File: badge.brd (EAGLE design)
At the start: 90.7 x 92.4 mm, 177 parts, among them CN4 MicroUSB, IC3 MEGA8-AI, Q1 BSS138, Q2 BSS138, T1 MMUN2133LT1G, U1 TPS61090RSAR, U2 MCP73871, U3 LIS3DHTR, U4 MIC5225-3.3, Y1 16.00MHz

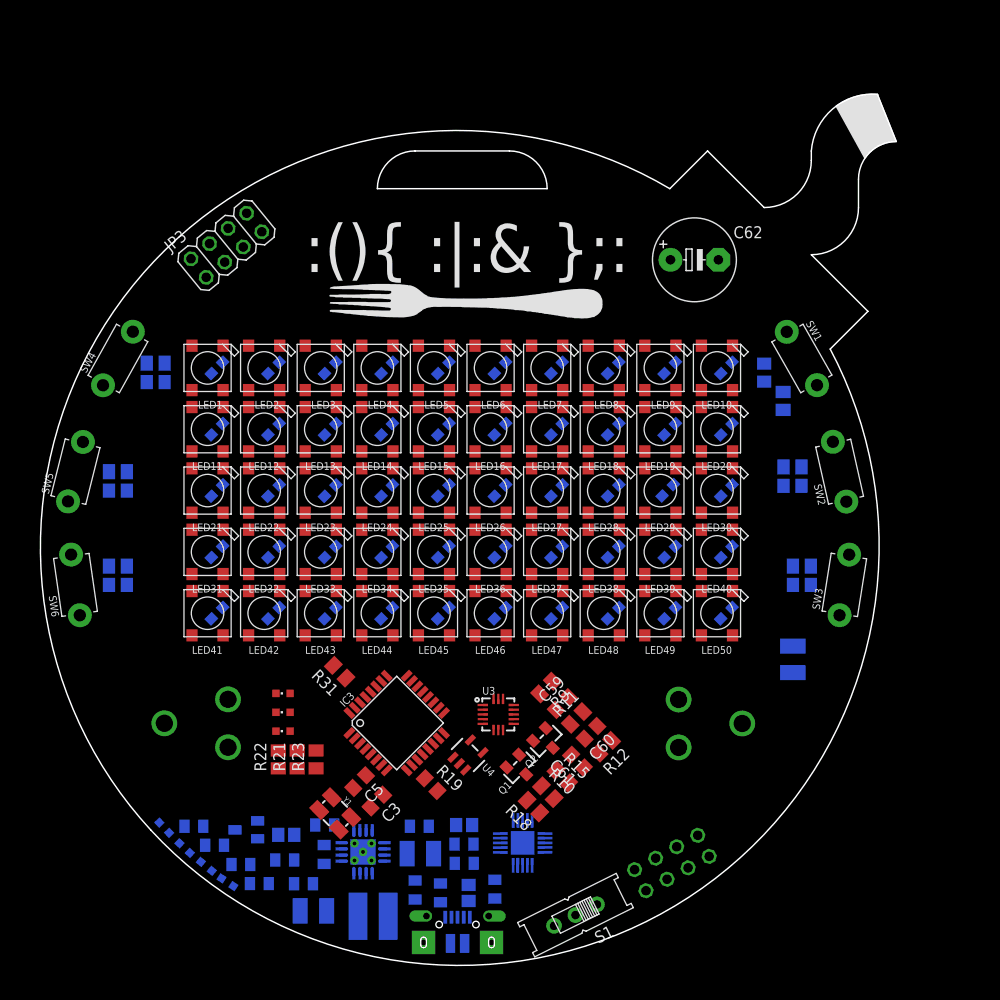
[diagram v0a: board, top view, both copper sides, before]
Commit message: Routed all the traces and performed a cursory DRC
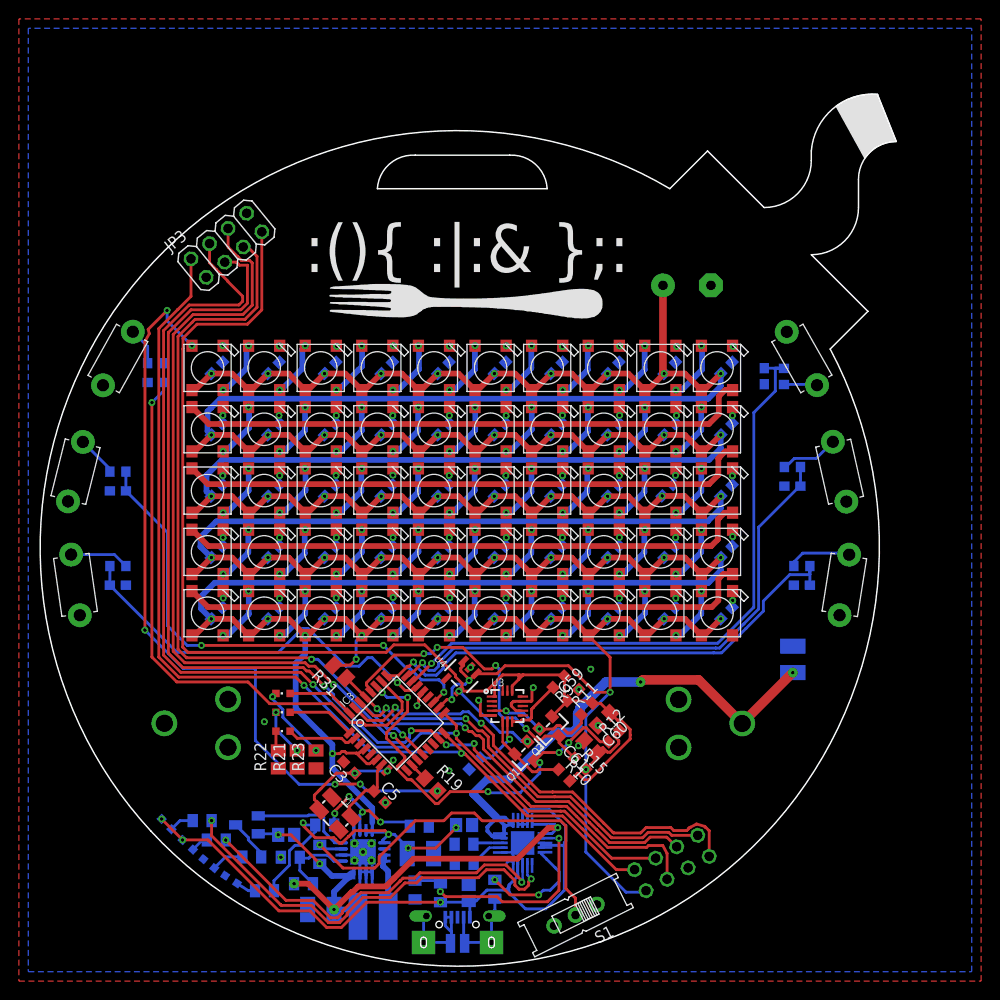
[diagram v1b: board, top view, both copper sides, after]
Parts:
- C3, C5, C59, C63, C64, C65, C66, C67, C68: device resistor:C0805 -> resistor:C0603
- R10, R11, R12, R15, R18, R24, R25, R26, R27, R28, R29, R9: device resistor:M0805 -> resistor:R0603
- moved U4 8.39 mm to (45.9, 31.3), turned to 135 degrees
- moved R18 7.70 mm to (47.3, 22.1), flipped to the bottom
- moved C3 4.61 mm to (34.0, 21.6), turned to 135 degrees
- moved C62 2.82 mm to (69.8, 72.8), flipped to the bottom, turned to 180 degrees
- moved C5 2.65 mm to (37.2, 18.5), turned to 315 degrees
- moved R24 2.60 mm to (80.1, 63.1)
- moved R10 2.50 mm to (56.8, 20.8)
- moved R15 2.33 mm to (58.5, 22.0)
- moved C61 2.05 mm to (59.6, 23.8)
- moved C60 1.94 mm to (61.0, 26.8)
- moved Q1 1.66 mm to (52.9, 23.0)
- moved R9 1.50 mm to (56.2, 30.7)
- moved R12 1.46 mm to (62.1, 25.0), turned to 45 degrees
- moved C59 1.45 mm to (57.7, 29.3)
- moved R11 1.45 mm to (59.2, 27.8)
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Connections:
- removed net CE\: JP3.6
- removed net PIEZO: IC3.13
- removed net VIN: C61.1, R12.2, R15.2, U4.1, U4.3
- new net CE: IC3.11, JP3.6
- net +5V: now also C61.1, R12.2, R15.2, U4.1, U4.3
- net CSN: now also IC3.12
- net GND: now also CN4.D+, CN4.D-, CN4.ID
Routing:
- net +5V: track 0.00 -> 734.5 mm, vias 0 -> 62
- net 3.3V: track 0.00 -> 132.4 mm, vias 0 -> 2
- net MOSI: track 0.00 -> 117.3 mm, vias 0 -> 4
- net SCK: track 0.00 -> 117.0 mm, vias 0 -> 2
- net MISO: track 0.00 -> 106.6 mm, vias 0 -> 2
- net CE: track 0.00 -> 83.6 mm, vias 0 -> 2
- net PIXEL_DATA: track 0.00 -> 82.2 mm, vias 0 -> 6
- net CSN: track 0.00 -> 80.6 mm, vias 0 -> 2
- net VBUS: track 0.00 -> 76.0 mm, vias 0 -> 3
- net SW1: track 0.00 -> 68.8 mm, vias 0 -> 1
- net SW4: track 0.00 -> 65.8 mm, vias 0 -> 1
- net N$71: track 0.00 -> 60.8 mm
- net N$61: track 0.00 -> 60.7 mm
- net N$41: track 0.00 -> 60.6 mm
- net N$51: track 0.00 -> 60.5 mm
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- added copper zone on layer 1, net GND
- added copper zone on layer 16, net GND
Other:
- outline, holes or cut-outs redrawn

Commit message: Routed all the traces and performed a cursory DRC
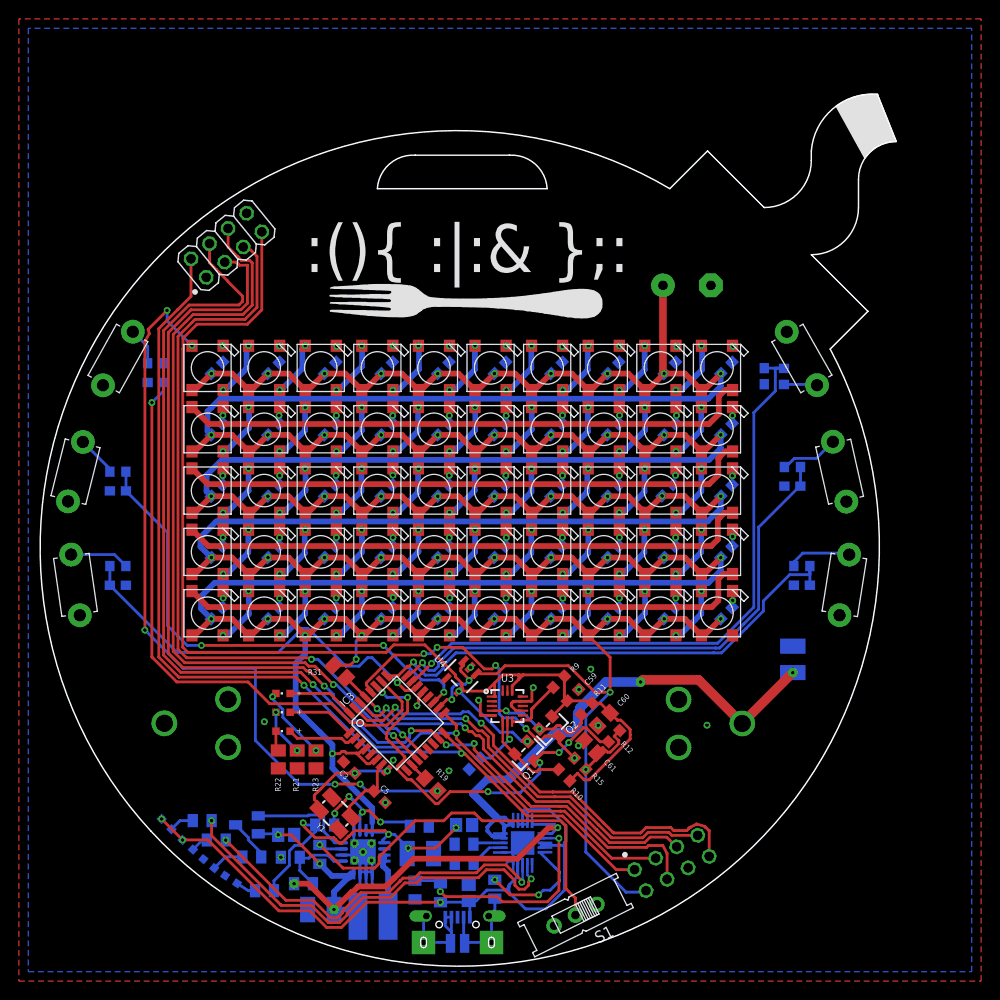
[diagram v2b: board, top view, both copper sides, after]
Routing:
- net GND: vias 63 -> 64
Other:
- board text added: "+"

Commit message: cleaned up the screenprinting
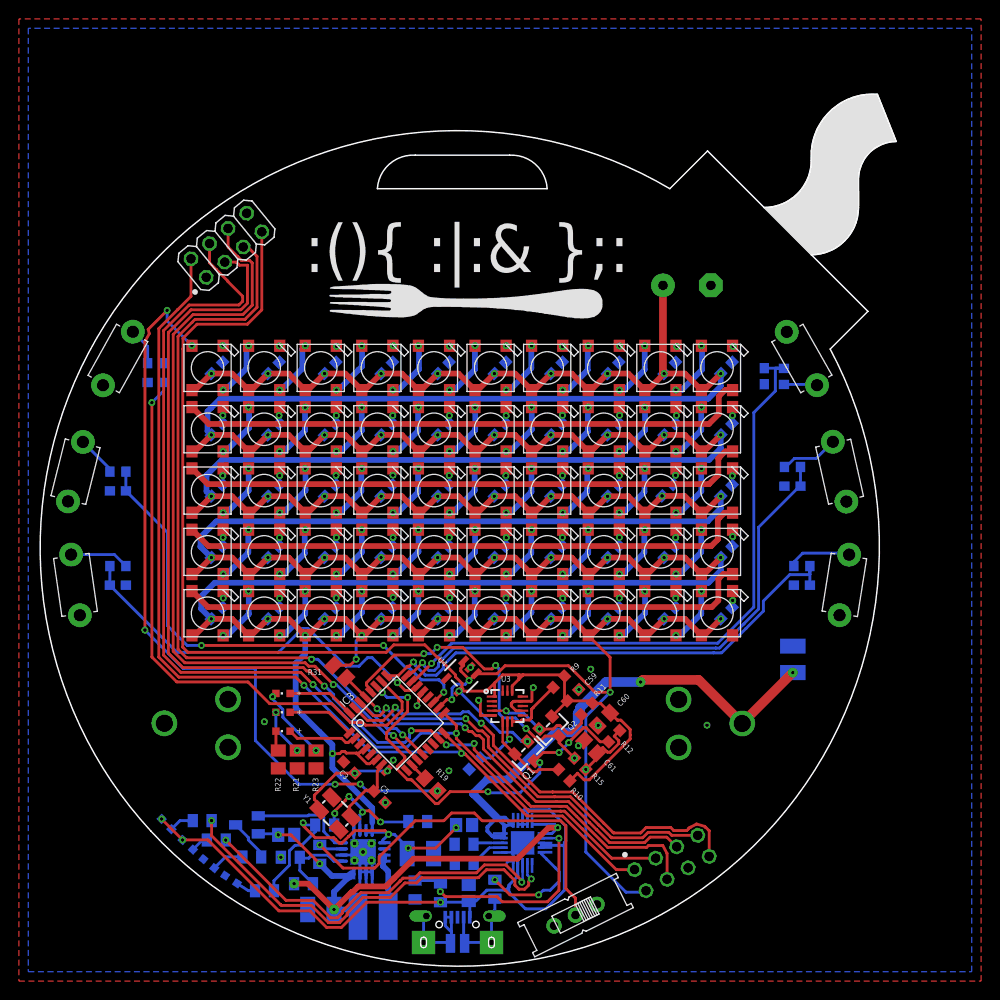
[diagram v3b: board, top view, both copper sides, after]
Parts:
- moved R4 0.53 mm to (41.3, 15.9)

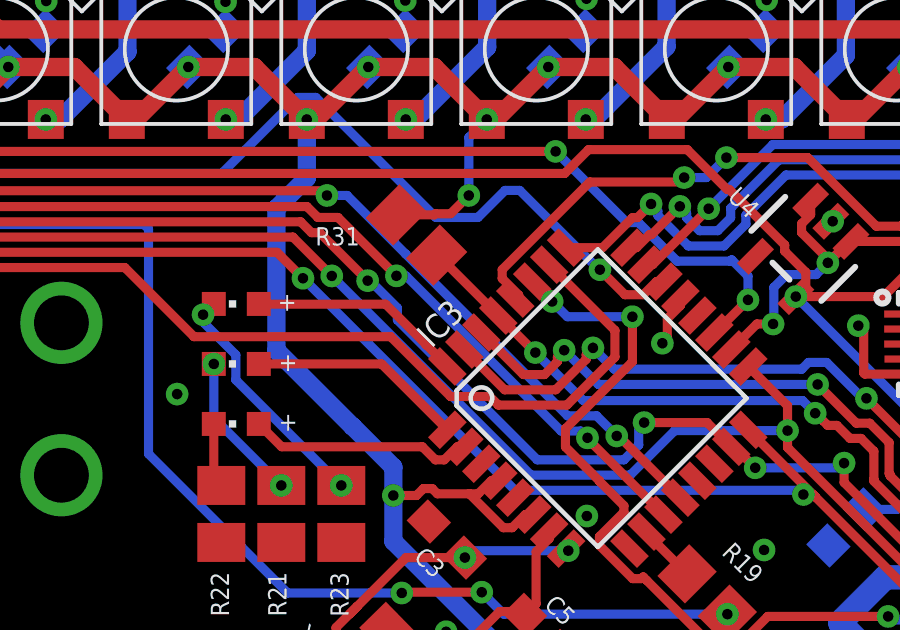
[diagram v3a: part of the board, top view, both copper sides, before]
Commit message: generated a BOM and started to add parts to it on digikey
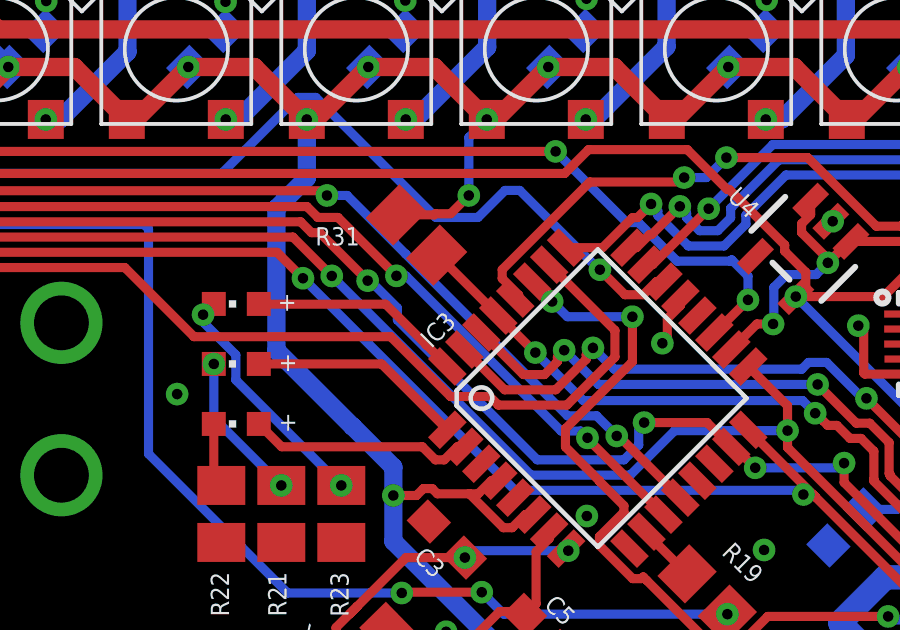
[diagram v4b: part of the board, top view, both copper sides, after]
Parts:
- C10, C11, C12, C13, C14, C15, C16, C17, C18, C19, C20, C21, C22, C23, C24, C25, C26, C27, C28, C29, C30, C31, C32, C33, C34, C35, C36, C37, C38, C39, C40, C41, C42, C43, C44, C45, C46, C47, C48, C49, C50, C51, C52, C53, C54, C55, C56, C57, C58, C9: value (none) -> 100nF

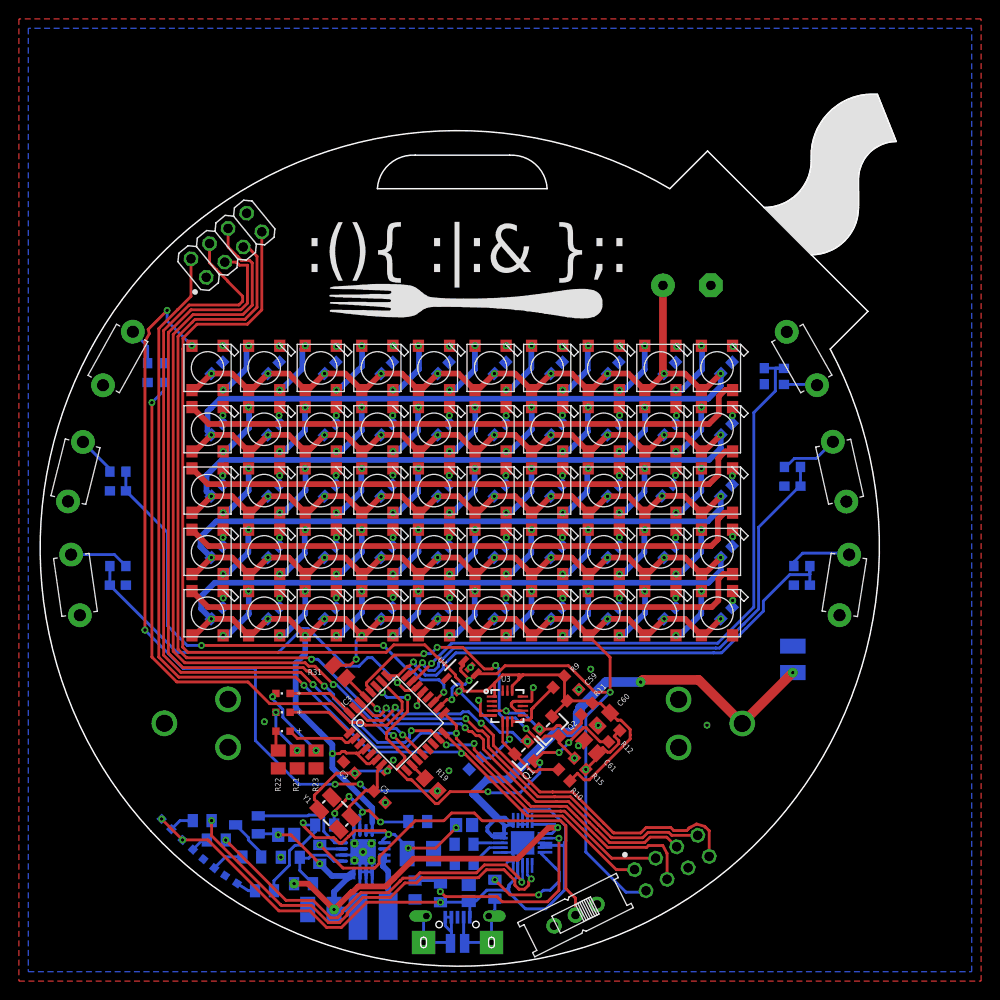
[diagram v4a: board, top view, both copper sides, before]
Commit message: cleaned up the traces and completed the BOM
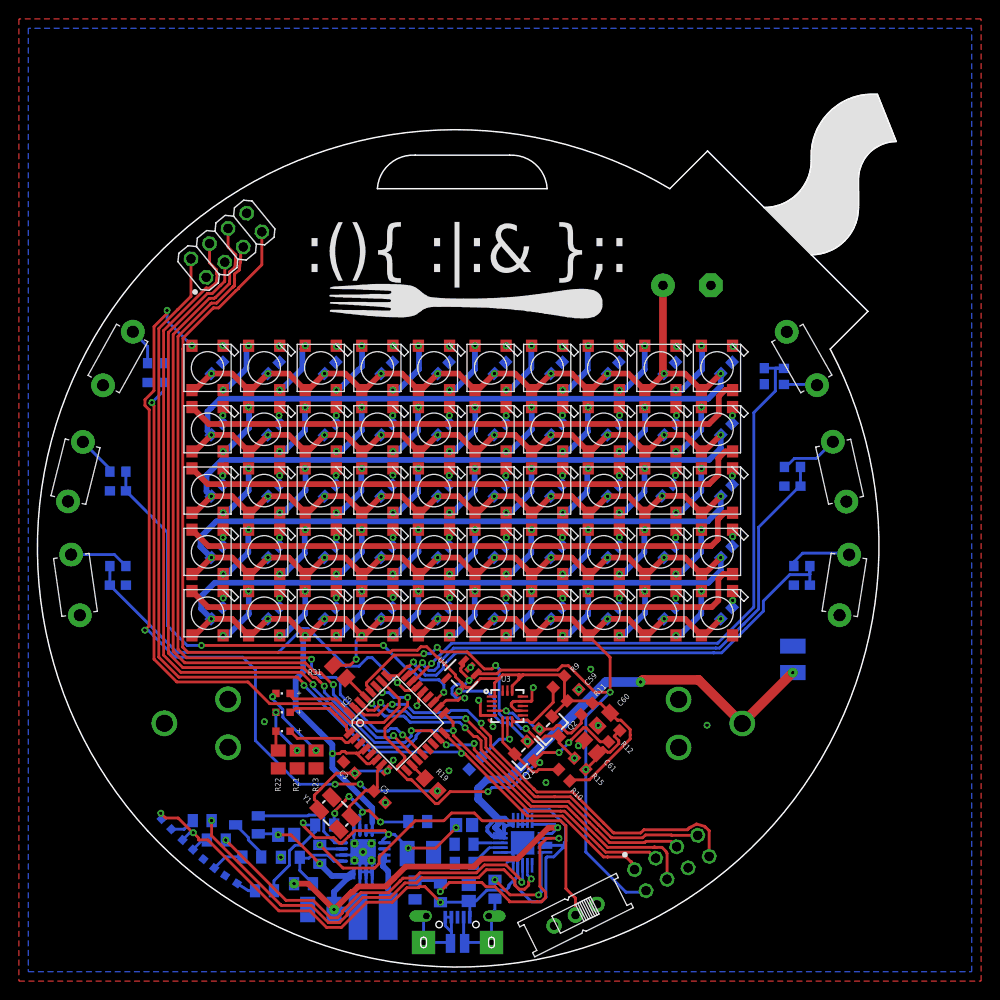
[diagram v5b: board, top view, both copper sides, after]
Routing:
- net MOSI: track 117.3 -> 111.2 mm
- net SCK: track 117.0 -> 112.0 mm
- net CE: track 83.6 -> 79.7 mm
- net VBUS: track 76.0 -> 79.1 mm
- net CSN: track 80.6 -> 78.1 mm
- net +5V: track 734.5 -> 736.8 mm
- net N$10: track 12.0 -> 9.92 mm
- net N$7: track 24.6 -> 26.4 mm
- net GND: track 52.6 -> 54.3 mm, vias 64 -> 66
- net 3.3V: track 132.4 -> 130.7 mm
- net SW4: track 65.8 -> 65.0 mm
- net VLIPO: track 58.4 -> 59.1 mm
- net N$19: track 6.64 -> 7.26 mm
- net STAT2: track 7.19 -> 7.82 mm
- net SDA: track 43.3 -> 42.7 mm
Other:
- board size 90.7 x 92.4 mm -> 91 x 92.5 mm
